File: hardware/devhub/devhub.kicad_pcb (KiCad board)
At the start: 4 copper layers, 100 x 100 mm, 154 parts, among them J1 USB-C PWR IN, J101 USB-C, J2 USB-C UPSTREAM, J201 USB-C, J301 USB-C, J4 SWD, J401 USB-C, J5 Banana COM 1, J6 Banana NC 1, J9 UART debug, K1 G5Q-1 DC5, SW1 relè on/off, SW101 porta on/off, SW201 porta on/off, SW301 porta on/off, SW401 porta on/off, U1 AP7361C-33E, U101 PI3USB4002A, U12 MCP120T-300I/TT, U13 TPS259470ARPWR, U2 USB2517I-JZX, U201 PI3USB4002A, U3 STM32G0B1CEU6, U301 PI3USB4002A, U4 UCS2114-1-V/LX, U401 PI3USB4002A, U5 UCS2114-1-V/LX, U9 ULN2003V12, Y1 24MHz 12pF

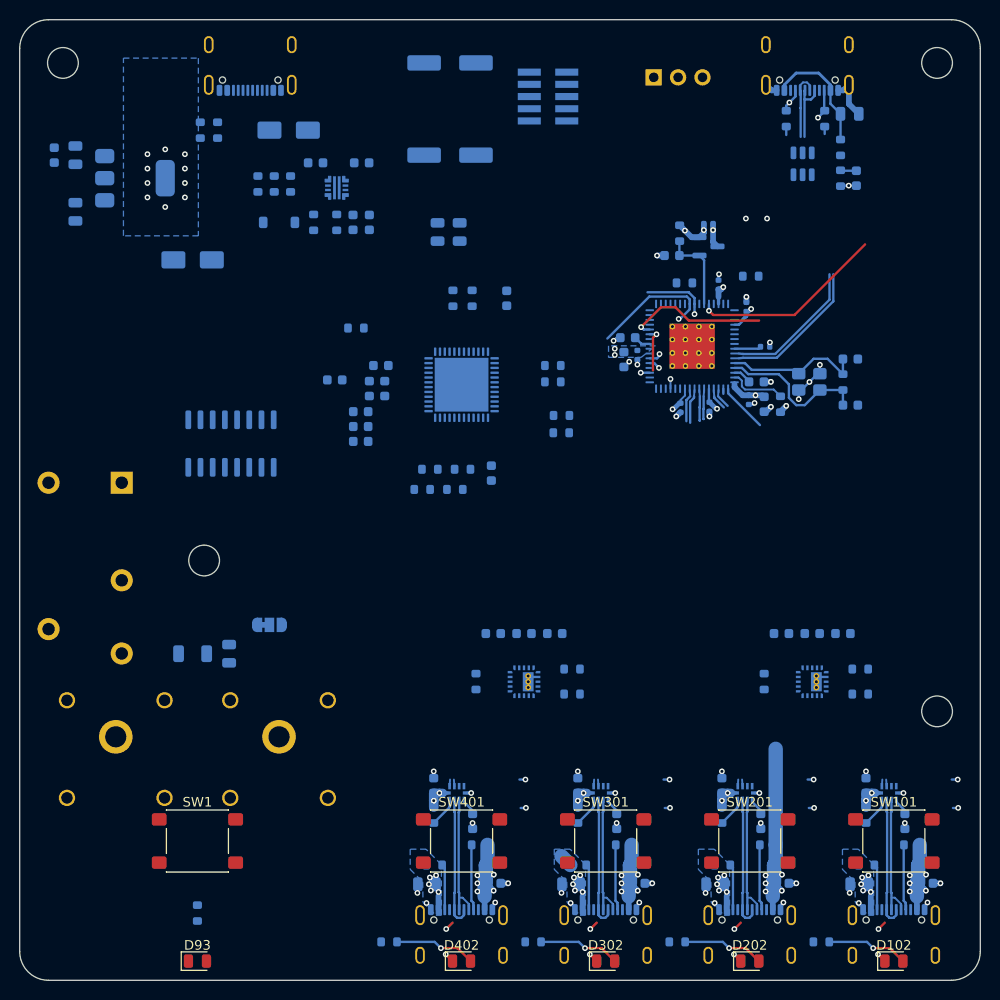
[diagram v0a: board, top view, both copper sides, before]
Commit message: MCU 100 nF caps in 0402, U2/U3 fanout rule areas (D88)
- C41, C42, C46 to C_0402_1005Metric, warehouse ID 217 (CC0402KRX7R7BB104)
- Single U2_FANOUT and new U3_FANOUT rule areas for USB clearance exceptions
- Zone defaults: 1 mm corner radius, 0.1 mm min clearance
- Fix MCU pin numbers in D57 (UFQFPN48)
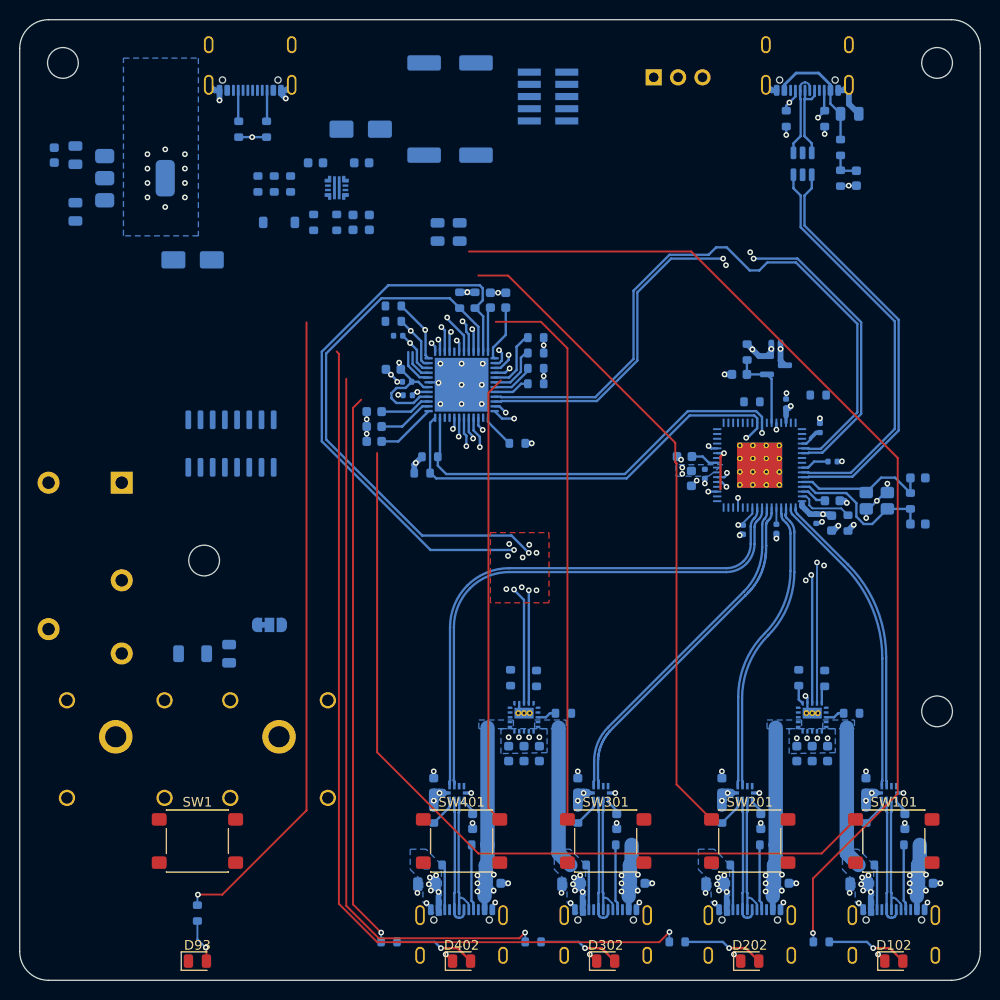
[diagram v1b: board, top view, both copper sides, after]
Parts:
- C41, C42, C46: footprint Capacitor_SMD:C_0603_1608Metric -> Capacitor_SMD:C_0402_1005Metric
- moved R51 19.8 mm to (107.9, 76.7), turned to -90 degrees
- moved C404 18.0 mm to (109.5, 76.7), turned to 90 degrees
- moved R50 17.6 mm to (106.3, 76.7), turned to -90 degrees
- moved C28 14.7 mm to (143.8, 90.0)
- moved C35 14.7 mm to (145.1, 97.6)
- moved C25 14.5 mm to (139.3, 100.5)
- moved C38 14.3 mm to (135.8, 100.6)
- moved C22 14.2 mm to (154.0, 100.0)
- moved C23 14.2 mm to (154.0, 95.2)
- moved C24 14.2 mm to (135.4, 84.4)
- moved C27 14.2 mm to (140.3, 87.5)
- moved C30 14.2 mm to (143.4, 99.5)
- moved C31 14.2 mm to (145.0, 99.9)
- moved C32 14.2 mm to (130.4, 95.2)
- moved C37 14.2 mm to (139.2, 81.1)
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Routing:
- net LED_P1: track 0.00 -> 109.7 mm, vias 0 -> 2
- net LED_P2: track 0.00 -> 96.4 mm, vias 0 -> 2
- net BTN_P1: track 0.00 -> 93.0 mm
- net LED_P3: track 0.00 -> 78.4 mm, vias 0 -> 2
- net I2C2_SDA: track 0.00 -> 77.5 mm, vias 0 -> 2
- net BTN_P2: track 0.00 -> 74.2 mm
- net I2C2_SCL: track 0.00 -> 72.7 mm, vias 0 -> 2
- net /MCU STM32G0B1/LED_HOST: track 0.00 -> 70.9 mm, vias 0 -> 1
- net USB_MCU_DN: track 0.00 -> 69.0 mm
- net USB_MCU_DP: track 0.00 -> 68.6 mm, vias 0 -> 2
- net BTN_P3: track 0.00 -> 63.0 mm
- net LED_P4: track 0.00 -> 59.8 mm, vias 0 -> 2
- net I2C1_SCL: track 18.4 -> 74.5 mm, vias 1 -> 2
- net HUB_DP4: track 4.11 -> 56.9 mm
- net HUB_DN4: track 4.28 -> 57.0 mm
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- added copper zone on B.Cu, net +5V
- added copper zone on F.Cu, net GND

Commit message: Restore relay LED, larger NC/NO jumper, PCB routing progress (D89, D90)
- D90/R90 relay LED back on RLY1, in the front LED row in line with SW1;
  host LED D93/R93 moved to the rear next to J1
- JP2: project footprint with 2.0x3.0 mm pads, 2.4 mm pitch and 1.0 mm
  bridge for 3 A relay contacts
- U13: 0.2 mm tracks from pads 8/9 alongside the corner pads, no clearance
  exception
- Routing and placement progress, zone defaults, schematic layout cleanup
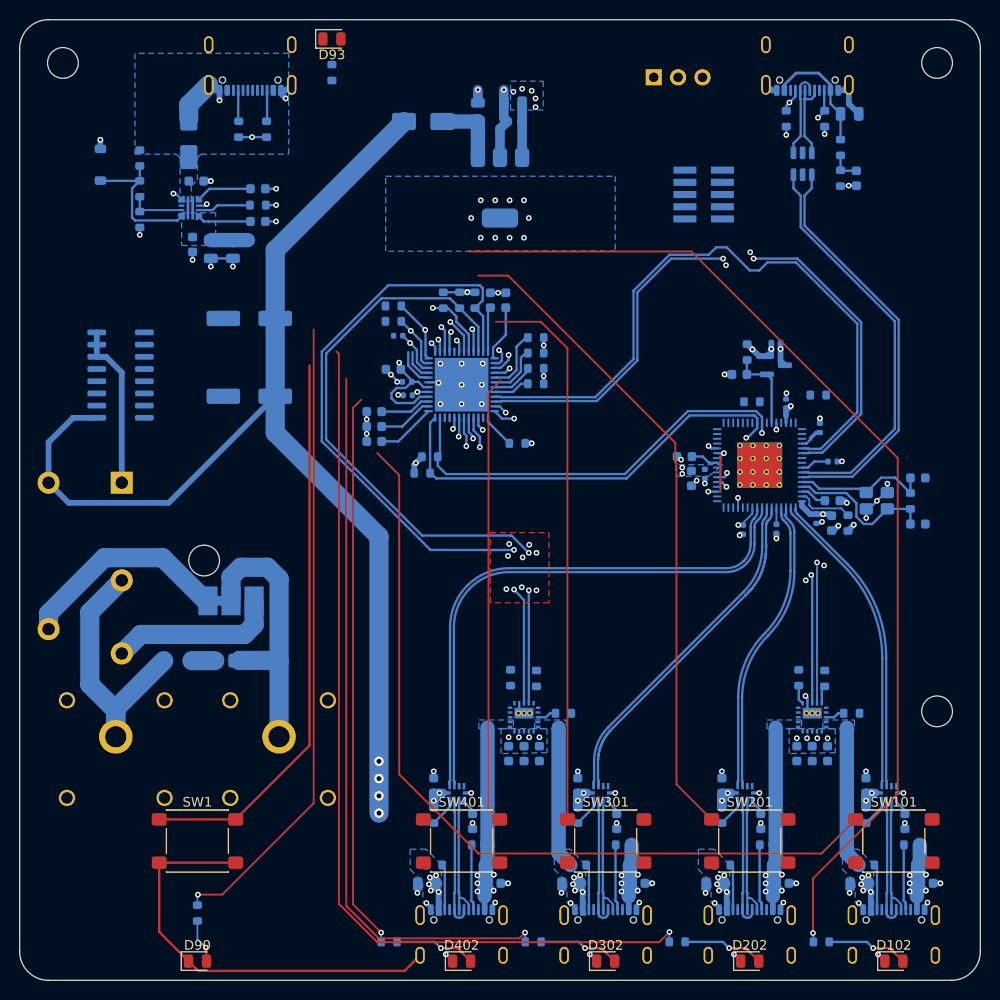
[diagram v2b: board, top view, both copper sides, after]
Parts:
- added D93: arancio, LED_SMD:LED_0805_2012Metric, F.Cu at (93.0, 49.5)
- added R93: 1k, Resistor_SMD:R_0603_1608Metric, B.Cu at (93.0, 53.0)
- D90: renamed from D93; value arancio -> verde
- JP2: footprint Jumper:SolderJumper-3_P1.3mm_Bridged12_RoundedPad1.0x1.5mm -> lcsc_footprints:SolderJumper-3_P2.4mm_Bridged12_Pad2.0x3.0mm
- moved C10 48.1 mm to (112.0, 58.1), turned to 180 degrees
- moved C9 45.9 mm to (111.8, 56.2), turned to 180 degrees
- moved C8 43.2 mm to (108.2, 57.1)
- moved C3 40.5 mm to (84.4, 86.7), turned to 180 degrees
- moved U1 38.0 mm to (110.5, 65.0), turned to -90 degrees
- moved D2 28.0 mm to (102.5, 58.1), turned to 180 degrees
- moved C4 26.9 mm to (84.4, 78.6), turned to 180 degrees
- moved C5 26.0 mm to (80.4, 71.4), turned to -90 degrees
- moved C6 21.4 mm to (82.7, 71.4), turned to -90 degrees
- moved C7 19.5 mm to (78.5, 70.9), turned to -90 degrees
- moved D4 19.5 mm to (68.9, 62.6), turned to 90 degrees
- moved J4 19.1 mm to (131.7, 65.7)
- moved D1 17.9 mm to (78.1, 59.8), turned to 90 degrees
- moved R30 15.9 mm to (73.0, 61.9), turned to -90 degrees
- moved R34 15.7 mm to (104.6, 76.7), turned to -90 degrees
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- renumbered R93 to R90
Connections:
- net /MCU STM32G0B1/LED_HOST_K renamed /Relè ausiliario/LED_RLY1_A
- R90 pad 1: /MCU STM32G0B1/LED_HOST -> RLY1
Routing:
- net +5V: track 0.00 -> 209.5 mm, vias 8 -> 12
- net GND: track 72.7 -> 142.2 mm, vias 96 -> 108
- net /MCU STM32G0B1/LED_HOST: track 70.9 -> 4.05 mm, vias 1 -> 0
- net RLY1: track 3.33 -> 69.8 mm, vias 1 -> 2
- net BTN_RLY1: track 5.89 -> 64.3 mm
- net /Relè ausiliario/BAN1_2: track 0.00 -> 29.7 mm
- net /Relè ausiliario/BAN1_COM: track 0.00 -> 28.8 mm
- net /Relè ausiliario/K1_NC: track 0.00 -> 22.5 mm
- net /Relè ausiliario/K1_NO: track 0.00 -> 17.5 mm
- net /Relè ausiliario/RLY1_COIL: track 0.00 -> 17.3 mm
- net /Alimentazione/EFUSE_EN: track 0.00 -> 15.2 mm
- net /Alimentazione/5V_LOGIC: track 0.00 -> 7.52 mm
- net +3V3: track 49.7 -> 57.0 mm, vias 20 -> 25
- net /Alimentazione/EFUSE_OV: track 0.00 -> 5.95 mm
- net /Alimentazione/EFUSE_DVDT: track 0.00 -> 5.82 mm
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- added copper zone on B.Cu, net /Alimentazione/VBUS_IN

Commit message: PCB routing complete, package in values, MPN fields
- Routing finished; ESD_FANOUT rule area for D20 centre pins
- Vias keep inner-layer rings only where connected; GND reference vias
  next to SWD and I2C layer changes
- Value field of chip R/C/LED includes the package (0402...1206)
- New fields MPN lcsc, MPN mouser, MPN digikey; LCSC codes for R60/R61,
  U3, U4/U5 and supplier codes completed; JP2 marked DNP on the PCB
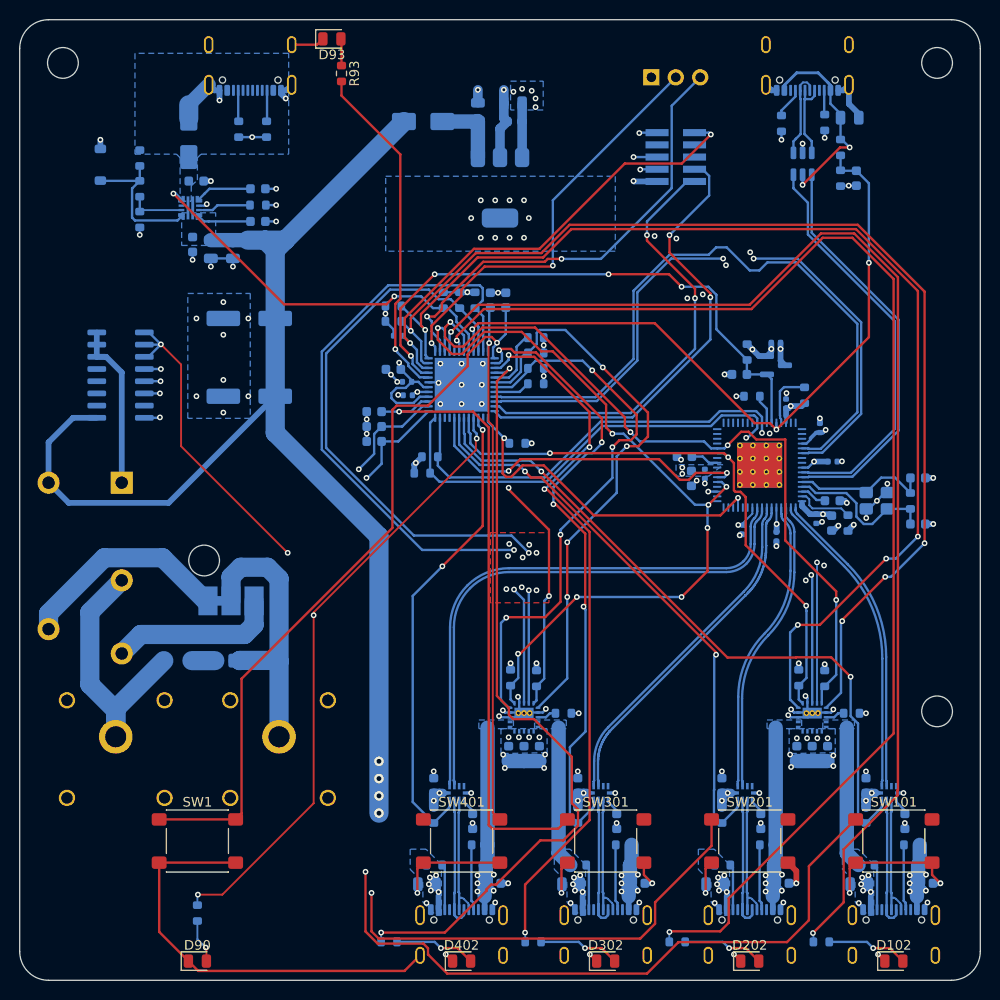
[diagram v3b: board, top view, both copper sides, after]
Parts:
- C10, C101, C103, C104, C201, C203, C204, C24, C301, C303, C304, C401, C403, C404, C60, C63, C83: value 100n -> 100n 0603
- C102, C202, C302, C402: value 22u 10V -> 22u 10V 0805
- C106, C206, C306, C406, C61, C62, C64, C65, C7: value 1u 25V -> 1u 25V 0603
- C11: value 2.2n -> 2.2n 0603
- C12: value 10n -> 10n 0603
- C13: value 100n 50V -> 100n 50V 0603
- C20: value 4.7u -> 4.7u 0805
- C21, C31, C32, C33, C35: value 1u -> 1u 0603
- C22, C23: value 15p C0G -> 15p C0G 0603
- C25, C26, C27, C28, C29, C30, C37, C38, C41, C42, C46: value 100n -> 100n 0402
- C40: value 4.7u -> 4.7u 0603
- C5, C6, C8, C9: value 10u -> 10u 0805
- C81: value 100n 50V DNP -> 100n 50V 0805 DNP
- D102, D202, D302, D402, D90: value verde -> verde 0805
- D93: value arancio -> arancio 0805
- R1, R2, R20, R21: value 5.1k -> 5.1k 0603
- R102, R103, R202, R203, R302, R303, R402, R403: value 56k -> 56k 0603
- R104, R204, R22, R23, R304, R404: value 100k -> 100k 0603
- R106, R206, R306, R406, R90: value 1k -> 1k 0603
- R24: value 1M -> 1M 0603
- R25: value 12.0k 1% -> 12.0k 1% 0603
- R26, R27, R28, R29, R34, R42, R43, R44, R45, R48, R49, R62, R63, R64, R65: value 10k -> 10k 0603
- R30: value 68.1k 1% -> 68.1k 1% 0603
- R31: value 8.66k 1% -> 8.66k 1% 0603
- R32: value 20.5k 1% -> 20.5k 1% 0603
- R33: value 953 1% -> 953 1% 0603
- R40, R41, R50, R51: value 4.7k -> 4.7k 0603
- R60, R61: value 27k 1% -> 27k 1% 0603
- R81: value 100 DNP -> 100 0.25W 1206 DNP
- R93: value 1k -> 1k 0603; moved to F.Cu
- moved J4 4.86 mm to (128.8, 61.8)
- moved R26 1.43 mm to (142.2, 86.6), turned to 90 degrees
- moved R93 1.00 mm to (94.0, 53.1), turned to 90 degrees
- moved C25 0.80 mm to (139.3, 101.3)
- moved R20 0.71 mm to (139.8, 58.3)
- moved R28 0.58 mm to (136.7, 86.7)
- moved C20 0.40 mm to (146.9, 57.7)
- moved R21 0.40 mm to (144.3, 58.2)
- moved J9 0.24 mm to (126.3, 53.5)
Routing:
- net EN_P2: track 6.90 -> 118.0 mm, vias 1 -> 4
- net EN_P1: track 5.81 -> 115.4 mm, vias 1 -> 4
- net GND: track 142.2 -> 233.0 mm, vias 108 -> 150
- net FAULT_P4: track 3.88 -> 82.6 mm, vias 2 -> 8
- net FAULT_P1: track 6.58 -> 79.3 mm, vias 2 -> 4
- net VBUS_DET: track 6.27 -> 74.2 mm, vias 2 -> 3
- net OE_N_P1: track 6.16 -> 72.0 mm, vias 1 -> 2
- net OE_N_P3: track 5.17 -> 66.1 mm, vias 1 -> 4
- net FAULT_P3: track 2.54 -> 62.0 mm, vias 2 -> 4
- net OE_N_P2: track 5.08 -> 59.8 mm, vias 1 -> 2
- net EN_P3: track 5.58 -> 59.5 mm, vias 0 -> 4
- net EN_P4: track 4.42 -> 58.3 mm, vias 0 -> 4
- net FAULT_P2: track 8.97 -> 61.3 mm, vias 2 -> 3
- net HUB_RST_N: track 12.1 -> 60.5 mm, vias 0 -> 4
- net /MCU STM32G0B1/UART_RX: track 1.41 -> 48.4 mm, vias 1 -> 2
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
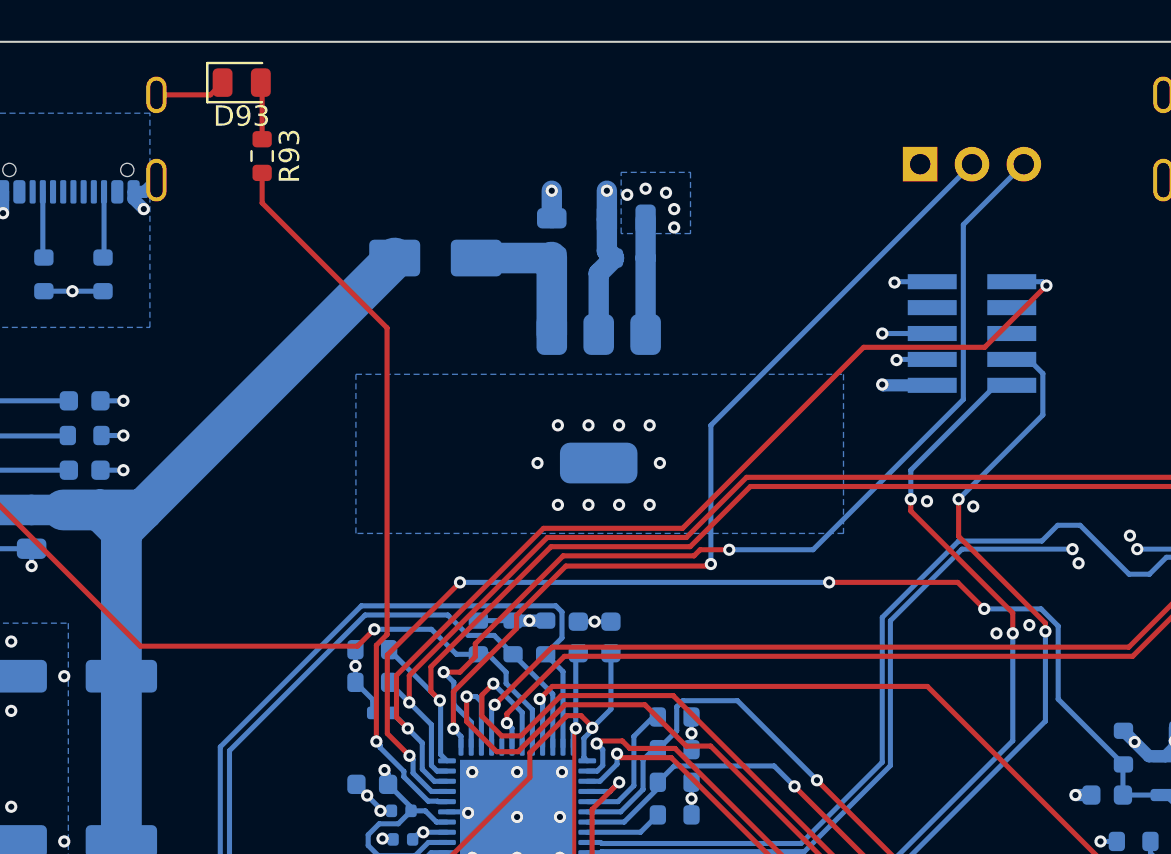
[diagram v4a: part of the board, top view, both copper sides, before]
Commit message: U1: switch to AP7361C-33ER (SOT-223R) for Mouser availability (D91)
- Project symbol devhub:AP7361C-33ER: pin 1 GND, pin 2 and tab OUT, pin 3 IN
- U1 supplier codes: LCSC C3743528, Mouser 621-AP7361C-33ER-13, DigiKey AP7361C-33ER-13DICT-ND
- PCB updated for the reversed pinout; U1_HEATSINK on +3V3
- Docs aligned: components, costs, architecture, PCB rules, decision D91
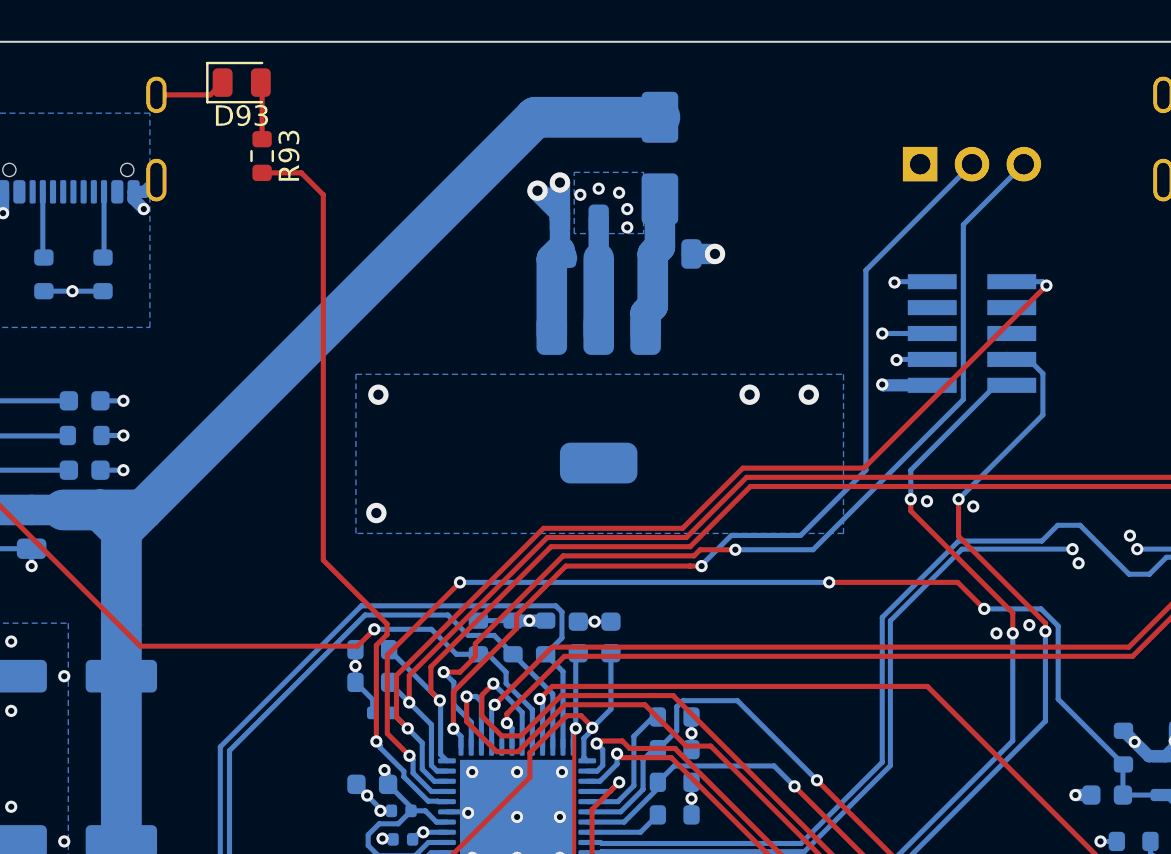
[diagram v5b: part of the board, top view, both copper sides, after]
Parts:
- U1: value AP7361C-33E -> AP7361C-33ER
- moved D2 12.0 mm to (113.5, 53.2), turned to 90 degrees
- moved C8 5.95 mm to (114.1, 57.9), turned to 0 degrees
- moved C10 2.30 mm to (109.7, 58.1)
- moved C9 2.30 mm to (109.5, 56.2)
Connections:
- U1 pad 1: /Alimentazione/5V_LOGIC -> GND
- U1 pad 2: GND -> +3V3
- U1 pad 3: +3V3 -> /Alimentazione/5V_LOGIC
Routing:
- net +5V: track 214.9 -> 230.7 mm
- net GND: track 233.0 -> 235.2 mm, vias 150 -> 141
- net /MCU STM32G0B1/UART_TX: track 43.4 -> 45.1 mm
- net /MCU STM32G0B1/LED_HOST: track 35.5 -> 36.7 mm
- net /Alimentazione/5V_LOGIC: track 7.52 -> 6.94 mm
- net +3V3: vias 33 -> 37
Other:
- board text added: "Check LDO pad connection"
